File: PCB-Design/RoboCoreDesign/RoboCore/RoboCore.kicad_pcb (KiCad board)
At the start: 4 copper layers, 68 x 60 mm, 80 parts, among them IC1 DRV8245SQRXZRQ1, IC2 DRV8245SQRXZRQ1, J1 SS-52400-002, J2 B2B-PH-SM4-TB, J3 MOTOR_A, J4 MOTOR_B, Q1 BC817, Q2 BC817, SW1 RESET, SW2 BOOT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

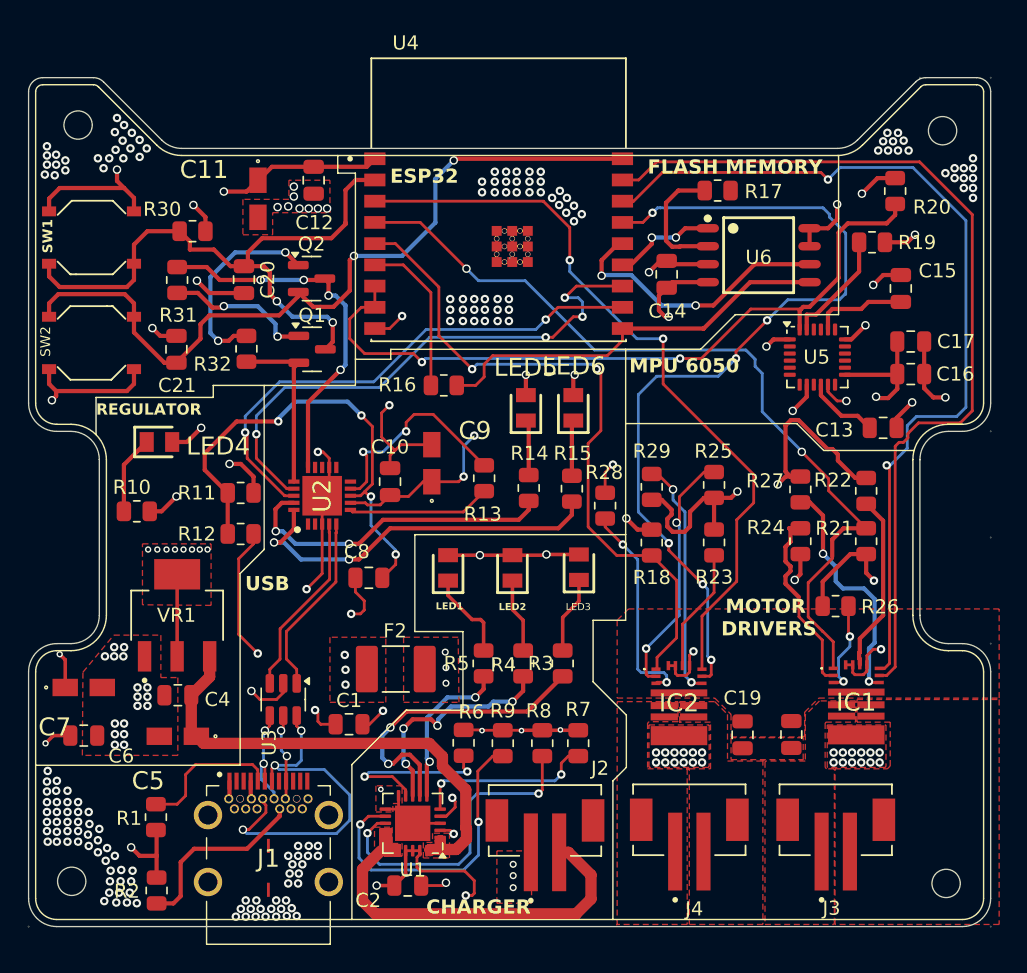
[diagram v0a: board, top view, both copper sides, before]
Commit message: Added board graphics
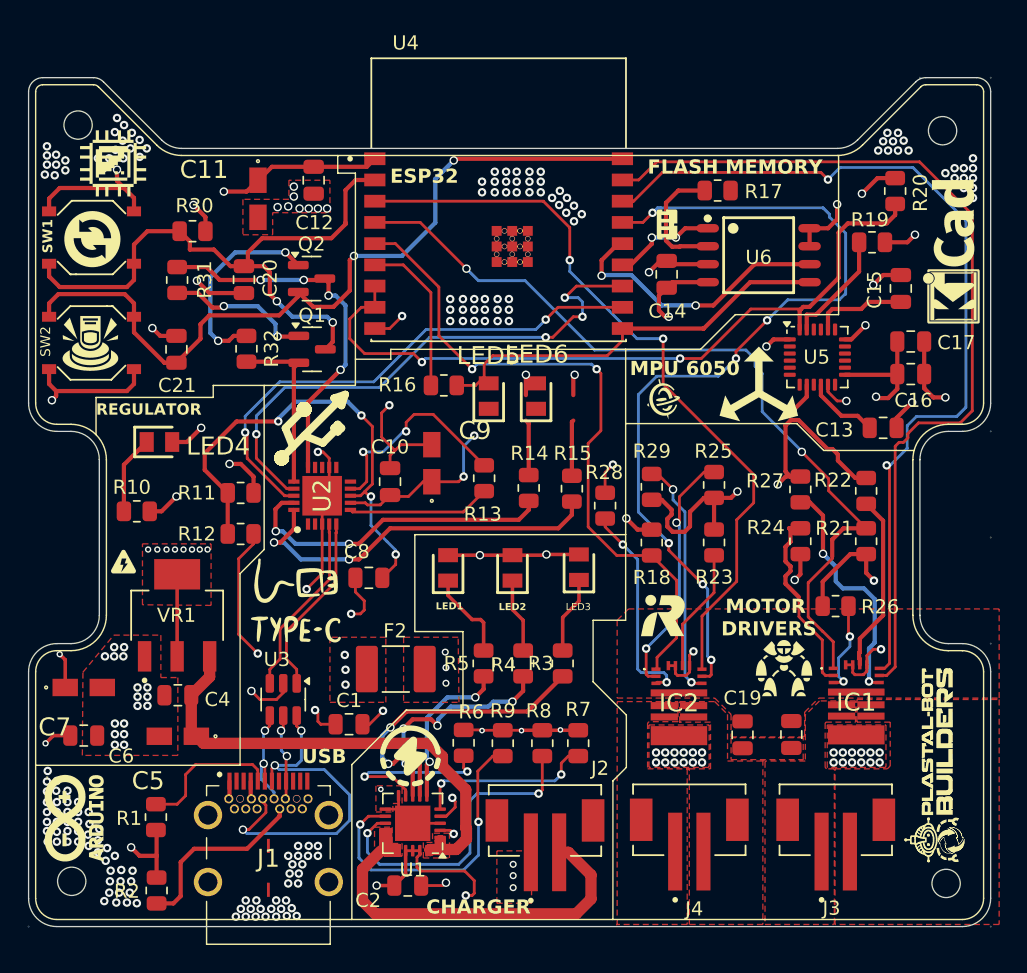
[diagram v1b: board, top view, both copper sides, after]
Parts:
- moved LED6 2.76 mm to (138.2, 84.1)
- moved LED5 2.76 mm to (134.8, 84.1)
